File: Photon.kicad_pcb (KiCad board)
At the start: 4 copper layers, 22.4 x 95.8 mm, 58 parts, among them J1 USB_C_Receptacle_USB2.0_14P, Q1 IRLML6402, Q2 IRLML6402, SW1 TS-1088-AR02016, U1 ATtiny13A-S, U2 RT8059GJ5, U3 TP4056, U4 BCR421UW6-7, U5 DW01A, U6 FS8205A, U7 BCR421UW6-7

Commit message: finished v3 of pcb
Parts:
- removed FID2, FID3: Fiducial, Fiducial:Fiducial_0.5mm_Mask1.5mm
- added G***: LOGO, Photon:Bugs_50mm, F.Cu at (52.8, 91.7)
- added G***: LOGO, Photon:bugs_side_40mm, B.Cu at (52.8, 61.8)
- moved R19 66.0 mm to (58.5, 35.8), turned to 0 degrees
- moved Q2 60.9 mm to (54.9, 37.0), turned to -90 degrees
- moved C7 29.4 mm to (47.4, 76.5)
- moved TP8 29.3 mm to (54.9, 69.3)
- moved R17 29.2 mm to (56.8, 73.0)
- moved U5 29.1 mm to (50.9, 75.8)
- moved U6 29.1 mm to (56.3, 75.8)
- moved R14 27.7 mm to (45.6, 74.9)
- moved U1 26.6 mm to (53.1, 103.1), turned to 0 degrees
- moved TP3 26.4 mm to (43.1, 98.6)
- moved TP9 26.4 mm to (43.1, 106.7)
- moved TP1 26.4 mm to (44.6, 108.7)
- moved TP2 26.4 mm to (44.6, 100.6)
- moved TP4 26.4 mm to (43.1, 102.6)
- moved TP5 26.4 mm to (44.6, 104.6)
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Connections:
- net /BAT_SAF_OUT renamed /Bat-
- net /PMOS_Gate renamed /USB_DSBL
- net /PMOS_OUT renamed /PMOS_EN_OUT
- net Net-(Q2-G) renamed /BAT_DSBL
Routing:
- net /Bat-: track 28.0 -> 102.2 mm, vias 1 -> 3
- net +3V3: track 23.5 -> 97.4 mm, vias 12 -> 4
- net /LED1_EN: track 23.2 -> 77.3 mm, vias 0 -> 4
- net /PMOS_EN_OUT: track 2.07 -> 43.3 mm, vias 0 -> 2
- net /BUCK_EN: track 37.8 -> 4.45 mm
- net PACK+: track 12.5 -> 41.6 mm, vias 4 -> 2
- net /Bat+: track 72.6 -> 45.7 mm, vias 1 -> 3
- net /MISO_BTN: track 56.4 -> 35.1 mm
- net 5V: track 23.4 -> 40.8 mm, vias 5 -> 0
- net GND: track 42.4 -> 32.9 mm, vias 23 -> 21
- net /MOSI: track 4.75 -> 12.9 mm
- net /LED2_EN: track 12.0 -> 20.1 mm, vias 0 -> 2
- net /SCK: track 4.96 -> 12.1 mm, vias 0 -> 2
- net /RESET: track 16.8 -> 20.7 mm
- net /OUT_LED1: track 7.99 -> 10.7 mm
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- added copper zone on B.Cu, net GND
- removed copper zone on F.Cu, net +3V3
- removed copper zone on In2.Cu, net +3V3
- removed copper zone on In2.Cu, net 5V
- removed copper zone on In1.Cu, net GND
- removed copper zone on B.Cu, net PACK+
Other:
- outline, holes or cut-outs redrawn
- copper layers 4 -> 2
- board text added: "K"
- board text removed: "SK"

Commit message: v1.3
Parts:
- removed G***: LOGO, Photon:Bugs_50mm
- removed G***: LOGO, Photon:bugs_side_40mm
- added FID2: Fiducial, Fiducial:Fiducial_0.5mm_Mask1.5mm, F.Cu at (59.9, 84.8)
- added FID3: Fiducial, Fiducial:Fiducial_0.5mm_Mask1.5mm, F.Cu at (44.7, 84.8)
- TP9: value 3V6 -> 3V3
- moved FID1 27.2 mm to (44.5, 41.1)
- moved R14 2.34 mm to (47.4, 73.4)
- moved TP6 0.80 mm to (59.4, 23.6)
- turned R19 to 180 degrees
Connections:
- C2 pad 2: PACK+ -> PACK_Safe
- C6 pad 2: PACK+ -> /Bat+
- Q1 pad 3: PACK+ -> PACK_Safe
- Q2 pad 2: PACK+ -> PACK_Safe
- R19 pad 1: /BAT_DSBL -> /Bat-
- R19 pad 2: /Bat- -> /BAT_DSBL
- U2 pad 4: PACK+ -> PACK_Safe
- U3 pad 5: PACK+ -> /Bat+
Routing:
- net PACK+: track 41.6 -> 0.00 mm, vias 2 -> 0
- net PACK_Safe: track 0.00 -> 35.6 mm, vias 0 -> 2
- net /Bat+: track 45.7 -> 48.5 mm
- net 5V: track 40.8 -> 39.9 mm
- net GND: track 32.9 -> 32.2 mm
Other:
- board text added: "Photon V3"

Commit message: Cleaned up PCB
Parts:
- removed D3: SZYY0603R1, LED_SMD:LED_0603_1608Metric
- removed R11: 300, Resistor_SMD:R_0603_1608Metric
- removed R3: 100K, Resistor_SMD:R_0603_1608Metric
- removed TP10: LED1_EN, TestPoint:TestPoint_Pad_D1.0mm
- removed TP11: LED2_EN, TestPoint:TestPoint_Pad_D1.0mm
- removed TP2: MOSI, TestPoint:TestPoint_Pad_D1.0mm
- removed TP3: RESET, TestPoint:TestPoint_Pad_D1.0mm
- removed TP4: MISO, TestPoint:TestPoint_Pad_D1.0mm
- removed TP5: SCK, TestPoint:TestPoint_Pad_D1.0mm
- removed TP6: 5V, TestPoint:TestPoint_Pad_D1.0mm
- added G***: LOGO, Photon:KAY Logo 10x10mm, F.Cu at (59.9, 79.8)
- added G***: LOGO, Photon:KAY Logo 10x10mm, B.Cu at (52.8, 51.1)
- added TP12: SCK, TestPoint:TestPoint_Pad_D1.0mm, F.Cu at (44.7, 62.5)
- added TP13: RESET, TestPoint:TestPoint_Pad_D1.0mm, F.Cu at (43.1, 56.4)
- BT1: footprint Photon:18650 Battery Holder -> Photon:Spring Battery TH
- R4: value 10K -> 100R
- R6: value 0R -> 100K
- TP7: value BTN -> MOSI
- TP8: value BuckEN -> MISO
- U4, U5, U6, U7: footprint Package_TO_SOT_SMD:SOT-23-6_Handsoldering -> Package_TO_SOT_SMD:SOT-23-6
- moved FID3 56.6 mm to (43.9, 28.2)
- moved TP7 55.5 mm to (44.7, 58.4), turned to -90 degrees
- moved R19 52.0 mm to (59.4, 87.8), turned to 90 degrees
- moved R18 42.3 mm to (52.3, 61.0), turned to 180 degrees
- moved TP9 42.2 mm to (43.2, 64.5)
- moved TP1 42.2 mm to (44.7, 66.5)
- moved C1 41.2 mm to (55.6, 61.0), turned to 180 degrees
- moved U1 38.4 mm to (51.3, 64.8)
- moved SW1 33.0 mm to (52.8, 80.8)
- moved U7 23.0 mm to (46.8, 77.2)
- moved R16 22.2 mm to (50.5, 78.0), turned to 0 degrees
- moved FID1 21.2 mm to (61.2, 28.2)
- moved R15 18.9 mm to (46.2, 80.0)
- moved D6 18.3 mm to (53.0, 72.6), turned to 180 degrees
- moved FID2 17.4 mm to (43.9, 91.7)
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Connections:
- C2 pad 2: PACK_Safe -> PACK_SAFE
- Q1 pad 1: /USB_DSBL -> /DSBL
- Q1 pad 2: /PMOS_EN_OUT -> PACK_SAFE
- Q1 pad 3: PACK_Safe -> /BUCK_EN
- Q2 pad 2: PACK_Safe -> PACK_SAFE
- R4 pad 1: 5V -> /DSBL
- R4 pad 2: /USB_DSBL -> 5V
- R5 pad 1: /USB_DSBL -> 5V
- R6 pad 2: /PMOS_EN_OUT -> GND
- TP7 pad 1: /MISO_BTN -> /MOSI
- TP8 pad 1: /BUCK_EN -> /MISO_BTN
- U2 pad 4: PACK_Safe -> PACK_SAFE
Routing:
- net /Bat-: track 102.0 -> 26.9 mm, vias 3 -> 0
- net /BAT_DSBL: track 1.96 -> 54.3 mm, vias 0 -> 2
- net /PMOS_EN_OUT: track 43.3 -> 0.00 mm, vias 2 -> 0
- net /LED1_EN: track 77.6 -> 41.4 mm
- net PACK_Safe: track 35.6 -> 0.00 mm, vias 2 -> 0
- net /BUCK_EN: track 4.45 -> 36.4 mm, vias 0 -> 2
- net /Bat+: track 48.5 -> 73.6 mm, vias 3 -> 2
- net PACK_SAFE: track 0.00 -> 24.6 mm, vias 0 -> 4
- net +3V3: track 97.4 -> 74.5 mm, vias 4 -> 2
- net /STAT1: track 2.65 -> 11.3 mm, vias 0 -> 2
- net /STAT2: track 2.44 -> 11.0 mm, vias 0 -> 2
- net /DSBL: track 0.00 -> 7.46 mm
- net /OUT_LED1: track 10.7 -> 17.3 mm, vias 0 -> 2
- net /USB_DSBL: track 6.49 -> 0.00 mm
- net /RESET: track 20.7 -> 14.4 mm, vias 0 -> 2
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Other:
- board size 22.4 x 95.8 mm -> 21.2 x 74.4 mm
- board text added: "Photon"
- board text removed: "3V3"
- board text removed: "GND"
- board text removed: "K"
- board text removed: "MI"
- board text removed: "MO"
- board text removed: "Photon V3"
- board text removed: "RST"

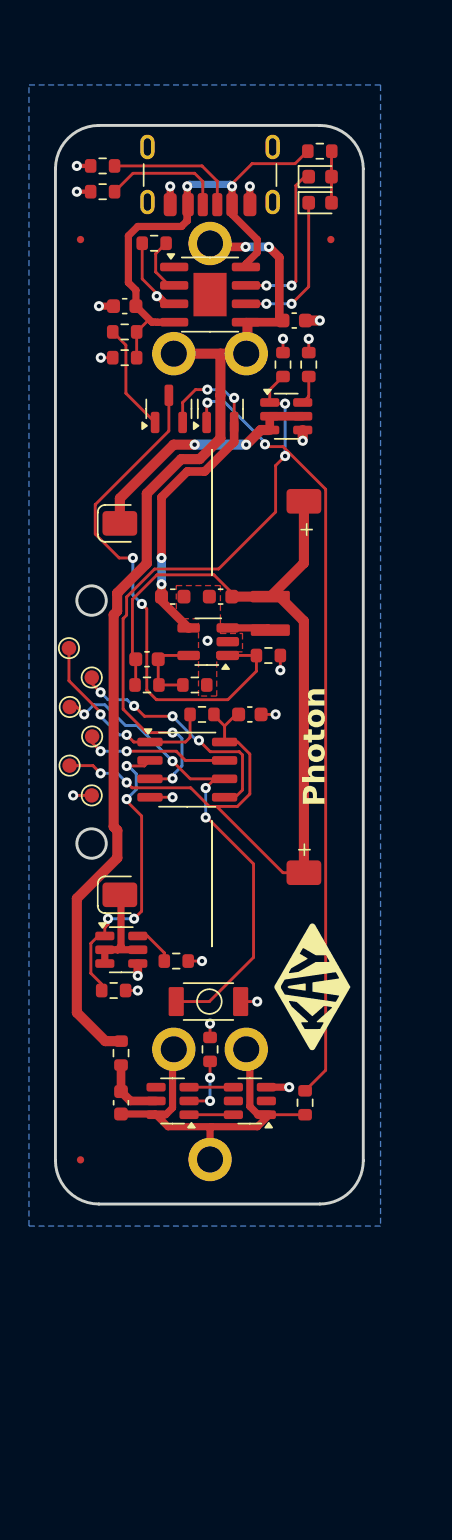
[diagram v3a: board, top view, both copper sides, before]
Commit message: made RT805 smaller footprint, moved few parts around and center tp4056 more over battery through holes
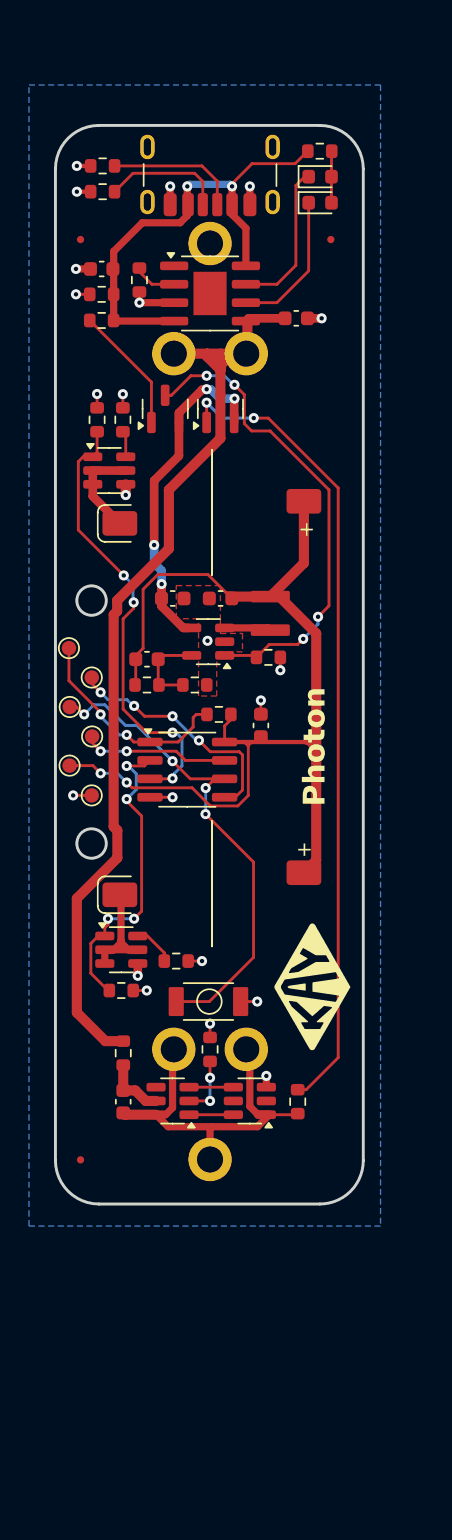
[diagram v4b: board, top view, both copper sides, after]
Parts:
- U2: footprint Package_TO_SOT_SMD:SOT-23-5_HandSoldering -> Package_TO_SOT_SMD:SOT-23-5
- moved R12 13.4 mm to (45.1, 40.6)
- moved R13 13.4 mm to (46.9, 40.6)
- moved U4 12.8 mm to (45.9, 44.1)
- moved R5 4.65 mm to (45.4, 32.0)
- moved C3 3.02 mm to (45.4, 30.2)
- moved R10 2.74 mm to (48.0, 31.0), turned to -90 degrees
- moved R4 1.77 mm to (45.4, 33.8)
- moved R18 1.17 mm to (53.5, 61.0)
- moved C1 1.08 mm to (56.4, 61.7), turned to -90 degrees
- moved R15 0.53 mm to (46.8, 80.0)
- moved R19 0.51 mm to (58.9, 87.7)
- moved Q1 0.25 mm to (49.8, 39.9)
- moved C6 0.21 mm to (58.8, 33.6)
- moved C7 0.17 mm to (46.9, 87.7)
- moved R14 0.15 mm to (46.9, 84.3)
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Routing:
- net /OUT_LED1: track 17.3 -> 6.71 mm, vias 2 -> 0
- net /LED1_EN: track 41.4 -> 31.6 mm
- net /Bat+: track 73.6 -> 66.3 mm, vias 2 -> 0
- net 5V: track 36.2 -> 33.0 mm
- net /BUCK_EN: track 36.4 -> 33.5 mm, vias 2 -> 4
- net GND: track 26.8 -> 24.0 mm
- net /OUT_LED2: track 7.36 -> 9.40 mm
- net /DSBL: track 7.46 -> 9.15 mm
- net /BAT_DSBL: track 54.3 -> 55.9 mm
- net /STAT2: track 11.0 -> 9.58 mm, vias 2 -> 0
- net PACK_SAFE: track 24.6 -> 23.2 mm
- net +3V3: track 74.5 -> 73.7 mm
- net /Iset: track 3.83 -> 3.06 mm
- net /STAT1: track 11.3 -> 10.6 mm, vias 2 -> 0
- net /Bat-: track 26.9 -> 26.2 mm
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
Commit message: small changed and exported .step
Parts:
- moved R18 4.94 mm to (58.4, 61.7), turned to 90 degrees
- moved R6 1.86 mm to (58.4, 58.2), turned to -90 degrees
- moved Q1 1.11 mm to (50.9, 40.2)
- moved Q2 1.11 mm to (54.7, 40.2)
- moved R15 0.72 mm to (46.9, 80.7), turned to -90 degrees
- moved G*** 0.31 mm to (60.2, 79.8)
- moved R14 0.25 mm to (46.9, 84.1)
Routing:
- net /Bat+: track 66.3 -> 73.9 mm, vias 0 -> 3
- net /RESET: track 15.0 -> 20.3 mm
- net +3V3: track 73.7 -> 71.6 mm
- net /BAT_DSBL: track 55.9 -> 54.6 mm
- net /BUCK_EN: track 33.5 -> 32.5 mm
- net /LED2_EN: track 21.9 -> 22.8 mm
- net /DSBL: track 9.15 -> 9.90 mm
- net PACK_SAFE: track 23.2 -> 22.7 mm

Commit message: gerbers and a few components moved
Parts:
- added FID2: Fiducial, Fiducial:Fiducial_0.5mm_Mask1.5mm, F.Cu at (61.3, 91.7)
- moved D1 6.43 mm to (58.8, 31.9)
- moved R7 6.43 mm to (58.8, 28.3)
- moved D2 6.43 mm to (58.8, 30.1)
- moved FID1 1.09 mm to (61.4, 27.1)
- moved FID3 1.09 mm to (44.1, 27.1)
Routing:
- net /STAT1: track 11.0 -> 3.53 mm
- net /STAT2: track 9.58 -> 2.97 mm
- net 5V: track 33.0 -> 30.5 mm
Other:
- board text added: "V4"
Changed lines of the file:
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@@
 			(drillshape 0)
 			(scaleselection 1)
-			(outputdirectory "Outputs/Gerbers/Photon V3/")
+			(outputdirectory "Outputs/Gerbers/Photon V4/")
 		)
 	)
@@
 	(footprint "Fiducial:Fiducial_0.5mm_Mask1.5mm"
 		(layer "F.Cu")
-		(at 43.942 28.194)
+		(at 44.1452 27.1272)
 		(descr "Circular Fiducial, 0.5mm bare copper, 1.5mm soldermask opening")
 		(tags "fiducial")
@@
 	(footprint "LED_SMD:LED_0603_1608Metric"
 		(layer "F.Cu")
-		(at 60.472 23.856)
+		(at 58.8264 30.0736)
 		(descr "LED SMD 0603 (1608 Metric), square (rectangular) end terminal, IPC-7351 nominal, (Body size source: http://www.tortai-tech.com/upload/download/2011102023233369053.pdf), generated with kicad-footprint-generator")
 		(tags "LED")
@@
 	(footprint "Resistor_SMD:R_0603_1608Metric"
 		(layer "F.Cu")
-		(at 60.452 22.098)
+		(at 58.8064 28.3156)
 		(descr "Resistor SMD 0603 (1608 Metric), square (rectangular) end terminal, IPC-7351 nominal, (Body size source: IPC-SM-782 page 72, https://www.pcb-3d.com/wordpress/wp-content/uploads/ipc-sm-782a_amendment_1_and_2.pdf), generated with kicad-footprint-generator")
 		(tags "resistor")
@@
 	(footprint "Fiducial:Fiducial_0.5mm_Mask1.5mm"
 		(layer "F.Cu")
-		(at 61.214 28.194)
+		(at 61.4172 27.1272)
 		(descr "Circular Fiducial, 0.5mm bare copper, 1.5mm soldermask opening")
 		(tags "fiducial")
@@
 	(footprint "LED_SMD:LED_0603_1608Metric"
 		(layer "F.Cu")
-		(at 60.472 25.654)
+		(at 58.8264 31.8716)
 		(descr "LED SMD 0603 (1608 Metric), square (rectangular) end terminal, IPC-7351 nominal, (Body size source: http://www.tortai-tech.com/upload/download/2011102023233369053.pdf), generated with kicad-footprint-generator")
 		(tags "LED")
@@
 		)
 	)
+	(footprint "Fiducial:Fiducial_0.5mm_Mask1.5mm"
+		(layer "F.Cu")
+		(at 61.2648 91.694)
+		(descr "Circular Fiducial, 0.5mm bare copper, 1.5mm soldermask opening")
+		(tags "fiducial")
+		(property "Reference" "FID2"
+			(at 0 -1.7 0)
+			(layer "F.SilkS")
+			(hide yes)
+			(effects
+				(font
+					(size 1 1)
+					(thickness 0.15)
+				)
+			)
+		)
+		(property "Value" "Fiducial"
+			(at 0 1.7 0)
+			(layer "F.Fab")
+			(effects
+				(font
+					(size 1 1)
+					(thickness 0.15)
+				)
+			)
+		)
+		(property "Datasheet" "~"
+			(at 0 0 0)
+			(layer "F.Fab")
+			(hide yes)
+			(effects
+				(font
+					(size 1.27 1.27)
+					(thickness 0.15)
+				)
+			)
+		)
+		(property "Description" "Fiducial Marker"
+			(at 0 0 0)
+			(layer "F.Fab")
+			(hide yes)
+			(effects
+				(font
+					(size 1.27 1.27)
+					(thickness 0.15)
+				)
+			)
+		)
+		(attr smd exclude_from_bom)
+		(fp_circle
+			(center 0 0)
+			(end 1 0)
+			(stroke
+				(width 0.05)
+				(type solid)
+			)
+			(fill no)
+			(layer "F.CrtYd")
+		)
+		(fp_circle
+			(center 0 0)
+			(end 0.75 0)
+			(stroke
+				(width 0.1)
+				(type solid)
+			)
+			(fill no)
+			(layer "F.Fab")
+		)
+		(fp_text user "${REFERENCE}"
+			(at 0 0 0)
+			(layer "F.Fab")
+			(effects
+				(font
+					(size 0.38 0.38)
+					(thickness 0.06)
+				)
+			)
+		)
+		(pad "" smd circle
+			(at 0 0)
+			(size 0.5 0.5)
+			(layers "F.Cu" "F.Mask")
+			(solder_mask_margin 0.5)
+			(clearance 0.5)
+		)
+		(embedded_fonts no)
+	)
 	(footprint "Photon:Spring Battery TH"
 		(layer "B.Cu")
@@
 		)
 	)
+	(gr_text "V4\n"
+		(at 48.1076 93.7768 0)
+		(layer "B.SilkS")
+		(effects
+			(font
+				(size 1.5 1.5)
+				(thickness 0.3)
+				(bold yes)
+			)
+			(justify left bottom mirror)
+		)
+	)
 	(segment
 		(start 46.8884 81.5462)
@@
 	)
 	(segment
-		(start 58.748 22.957)
-		(end 55.783 22.957)
+		(start 55.3538 28.2956)
+		(end 55.3538 28.6004)
+		(width 0.5)
+		(layer "F.Cu")
+		(net 15)
+	)
+	(segment
+		(start 55.3538 28.6004)
+		(end 55.3538 30.0094)
+		(width 0.5)
+		(layer "F.Cu")
+		(net 15)
+	)
+	(segment
+		(start 55.6786 28.3156)
+		(end 55.3538 27.9908)
 		(width 0.2)
 		(layer "F.Cu")
@@
 	)
 	(segment
-		(start 59.627 22.098)
-		(end 59.607 22.098)
+		(start 57.9814 28.3156)
+		(end 55.8292 28.3156)
 		(width 0.2)
 		(layer "F.Cu")
@@
 	)
 	(segment
+		(start 55.8292 28.3156)
+		(end 55.6386 28.3156)
+		(width 0.2)
+		(layer "F.Cu")
+		(net 15)
+	)
+	(segment
 		(start 51.308 26.543)
 		(end 51.308 24.4268)
@@
 	)
 	(segment
-		(start 59.607 22.098)
-		(end 58.748 22.957)
+		(start 55.6386 28.3156)
+		(end 55.3538 28.6004)
 		(width 0.2)
 		(layer "F.Cu")
@@
 	)
 	(segment
-		(start 50.4038 33.8194)
-		(end 46.2709 33.8194)
+		(start 55.3538 27.9908)
+		(end 55.3538 28.2956)
 		(width 0.5)
 		(layer "F.Cu")
@@
 	)
 	(segment
-		(start 54.3988 24.3412)
-		(end 54.3988 24.526)
-		(width 0.2)
+		(start 50.4038 33.8194)
+		(end 46.2709 33.8194)
+		(width 0.5)
 		(layer "F.Cu")
 		(net 15)
@@
 	)
 	(segment
-		(start 55.783 22.957)
-		(end 54.3988 24.3412)
+		(start 55.8292 28.3156)
+		(end 55.3738 28.3156)
+		(width 0.2)
+		(layer "F.Cu")
+		(net 15)
+	)
+	(segment
+		(start 55.8292 28.3156)
+		(end 55.6786 28.3156)
 		(width 0.2)
 		(layer "F.Cu")
@@
 	(segment
 		(start 55.3538 27.4138)
-		(end 55.3538 30.0094)
+		(end 55.3538 27.9908)
 		(width 0.5)
 		(layer "F.Cu")
@@
 	)
 	(segment
+		(start 55.3738 28.3156)
+		(end 55.3538 28.2956)
+		(width 0.2)
+		(layer "F.Cu")
+		(net 15)
+	)
+	(segment
 		(start 50.814 27.037)
 		(end 51.308 26.543)
@@
 	)
 	(segment
-		(start 61.2595 22.1155)
-		(end 61.2595 25.3975)
-		(width 0.2)
-		(layer "F.Cu")
-		(net 19)
-	)
-	(segment
-		(start 61.2595 25.3975)
-		(end 61.003 25.654)
-		(width 0.2)
-		(layer "F.Cu")
-		(net 19)
-	)
-	(segment
-		(start 61.277 22.098)
-		(end 61.2595 22.1155)
-		(width 0.2)
-		(layer "F.Cu")
-		(net 19)
-	)
-	(segment
-		(start 61.257 22.098)
-		(end 61.277 22.098)
+		(start 59.6139 28.3331)
+		(end 59.6139 31.6151)
 		(width 0.2)
 		(layer "F.Cu")
@@
 	)
 	(segment
-		(start 55.8426 32.5494)
-		(end 57.4936 32.5494)
-		(width 0.2)
-		(layer "F.Cu")
-		(net 20)
-	)
-	(segment
-		(start 55.765 32.627)
-		(end 55.8426 32.5494)
-		(width 0.2)
-		(layer "F.Cu")
-		(net 20)
-	)
-	(segment
-		(start 59.6845 30.3585)
-		(end 59.6845 25.654)
-		(width 0.2)
-		(layer "F.Cu")
-		(net 20)
-	)
-	(segment
-		(start 57.4936 32.5494)
-		(end 59.6845 30.3585)
+		(start 57.3611 32.5494)
+		(end 58.0389 31.8716)
 		(width 0.2)
 		(layer "F.Cu")
@@
 	)
 	(segment
-		(start 59.6845 25.654)
-		(end 59.6645 25.654)
+		(start 55.3538 32.5494)
+		(end 57.3611 32.5494)
 		(width 0.2)
 		(layer "F.Cu")
@@
 	)
 	(segment
-		(start 55.648 31.496)
-		(end 57.7088 31.496)
-		(width 0.2)
-		(layer "F.Cu")
-		(net 21)
-	)
-	(segment
-		(start 58.801 30.4038)
-		(end 58.801 24.4655)
-		(width 0.2)
-		(layer "F.Cu")
-		(net 21)
-	)
-	(segment
-		(start 58.801 24.4655)
-		(end 59.4105 23.856)
+		(start 55.3538 31.2794)
+		(end 57.415 31.2794)
 		(width 0.2)
 		(layer "F.Cu")
@@
 	)
 	(segment
-		(start 55.4314 31.2794)
-		(end 55.648 31.496)
+		(start 57.415 31.2794)
+		(end 58.0389 30.6555)
 		(width 0.2)
 		(layer "F.Cu")
@@
 	)
 	(segment
-		(start 57.7088 31.496)
-		(end 58.801 30.4038)
-		(width 0.2)
-		(layer "F.Cu")
-		(net 21)
-	)
-	(segment
-		(start 59.4105 23.856)
-		(end 59.6845 23.856)
+		(start 58.0389 30.6555)
+		(end 58.0389 30.0736)
 		(width 0.2)
 		(layer "F.Cu")
@@
 	)
 	(segment
-		(start 56.9976 30.83088)
-		(end 56.9976 29.75339)
-		(width 0.6)
-		(layer "F.Cu")
-		(net 31)
-	)
-	(segment
-		(start 56.98248 30.846)
-		(end 56.9976 30.83088)
-		(width 0.6)
-		(layer "F.Cu")
-		(net 31)
-	)
-	(segment
 		(start 52.2224 43.2816)
 		(end 53.594 43.2816)
@@
 	)
 	(segment
-		(start 56.9976 29.75339)
-		(end 56.40361 29.1594)
-		(width 0.6)
-		(layer "F.Cu")
-		(net 31)
-	)
-	(segment
 		(start 46.228 54.078937)
 		(end 46.471 53.835937)
@@
 	)
 	(segment
+		(start 56.40361 29.1594)
+		(end 56.1538 29.1594)
+		(width 0.6)
+		(layer "F.Cu")
+		(net 31)
+	)
+	(segment
 		(start 43.688 73.5076)
 		(end 46.482 70.7136)
@@
 	)
 	(segment
-		(start 56.40361 29.1594)
-		(end 56.1538 29.1594)
-		(width 0.6)
-		(layer "F.Cu")
-		(net 31)
-	)
-	(segment
 		(start 46.482 67.7164)
 		(end 46.228 67.4624)
@@
 	)
 	(segment
+		(start 56.9976 29.75339)
+		(end 56.40361 29.1594)
+		(width 0.6)
+		(layer "F.Cu")
+		(net 31)
+	)
+	(segment
+		(start 56.9976 30.5308)
+		(end 56.9976 29.75339)
+		(width 0.6)
+		(layer "F.Cu")
+		(net 31)
+	)
+	(segment
 		(start 53.594 43.2816)
 		(end 54.6608 42.2148)
@@
 	)
 	(via
-		(at 56.98248 30.846)
+		(at 56.9976 30.5308)
 		(size 0.7)
 		(drill 0.3)
@@
 	)
 	(segment
-		(start 56.98248 30.846)
-		(end 56.9976 30.86112)
-		(width 0.6)
-		(layer "B.Cu")
-		(net 31)
-	)
-	(segment
-		(start 56.9976 30.86112)
+		(start 56.9976 30.5308)
 		(end 56.9976 33.4398)
 		(width 0.6)

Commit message: Updated
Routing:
- net GND: track 24.0 -> 0.74 mm, vias 22 -> 23
- net /Bat+: track 73.9 -> 74.5 mm
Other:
- rule pad_to_mask_clearance: 0 -> 0.1
